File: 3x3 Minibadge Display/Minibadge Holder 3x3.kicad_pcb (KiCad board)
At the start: 2 copper layers, 82.5 x 82.6 mm, 32 parts, among them J1 TYPE-C-31-M-17, SW1 SW_SPDT, U1 AP2112K-3.3, U2 74HC4060, U3 TPM8837C

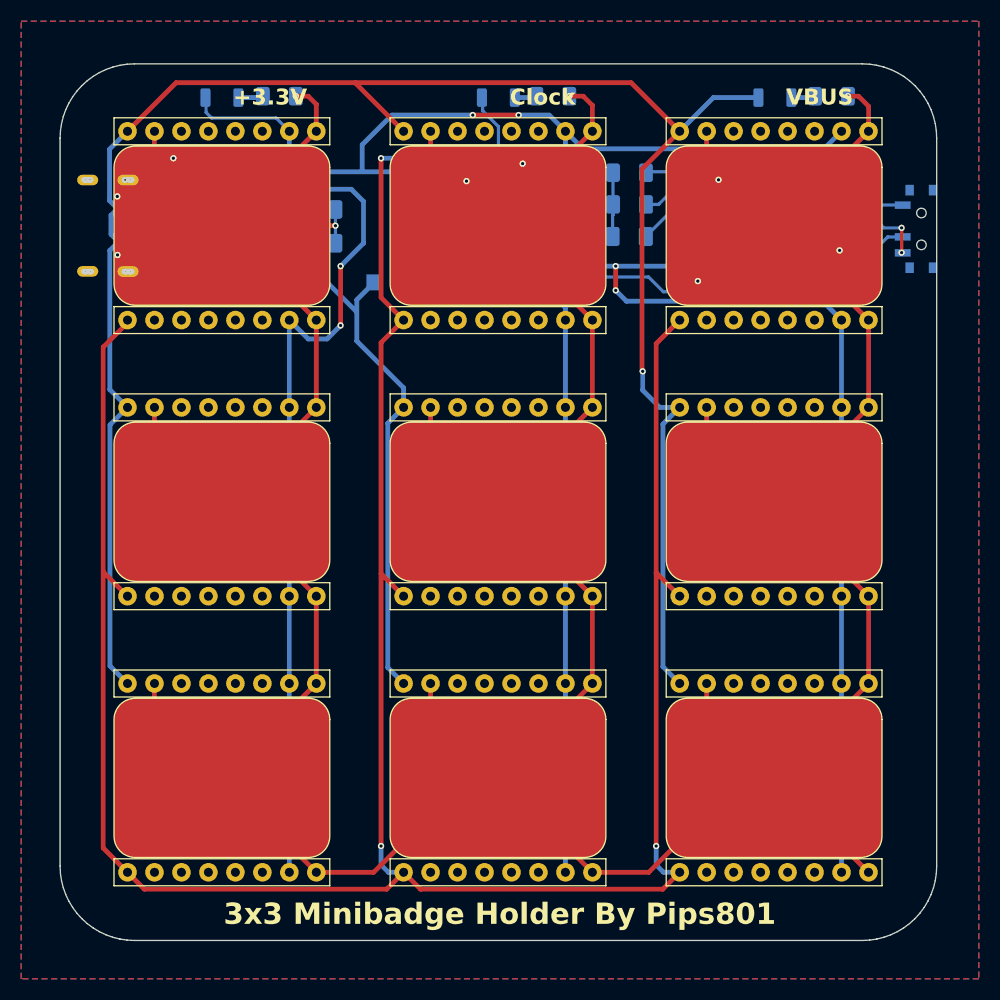
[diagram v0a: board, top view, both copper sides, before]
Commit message: r3 (on/off, graphics, laser cut files)
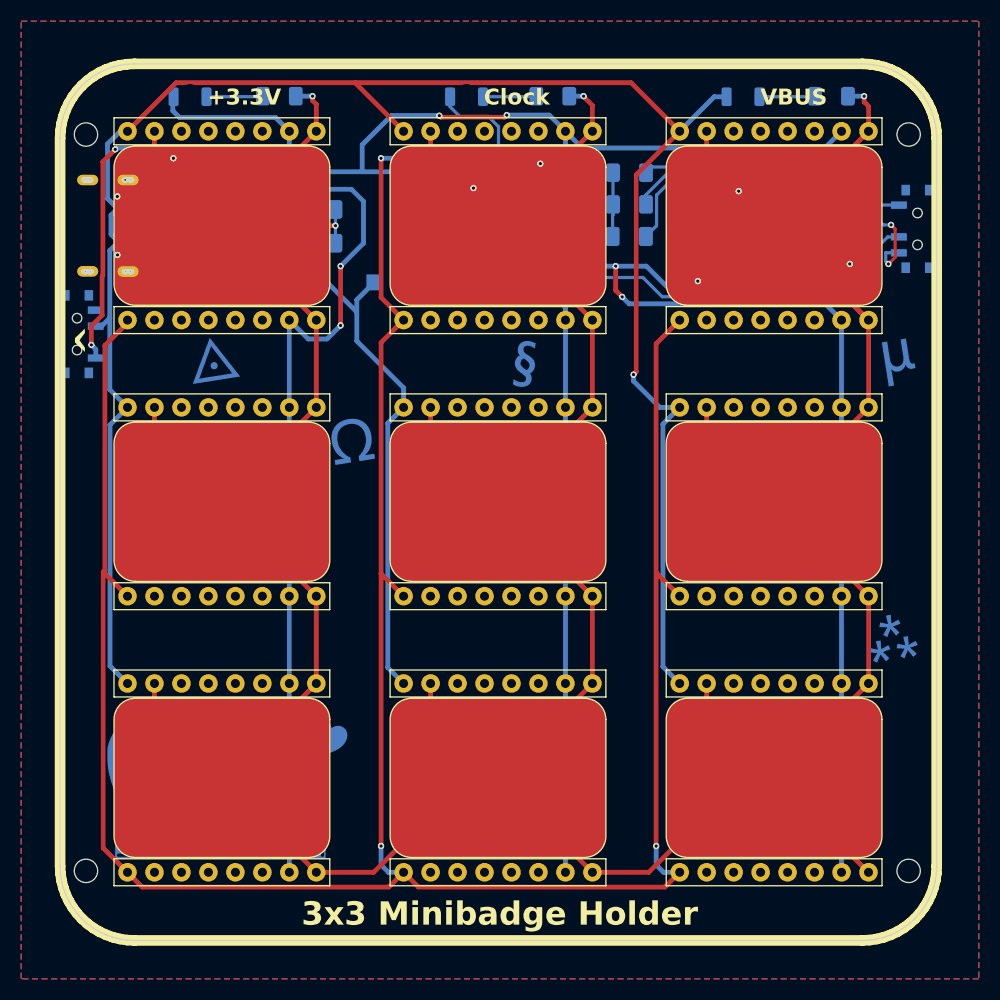
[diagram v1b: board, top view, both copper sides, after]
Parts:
- added G***: LOGO, LOGO, B.Cu at (179.4, 103.0)
- added G***: LOGO, LOGO, B.Cu at (123.5, 118.2)
- added REF**: MountingHole_2.2mm_M2, MountingHole:MountingHole_2.2mm_M2, F.Cu at (191.5, 65.3)
- added REF**: MountingHole_2.2mm_M2, MountingHole:MountingHole_2.2mm_M2, F.Cu at (114.0, 134.6)
- added REF**: MountingHole_2.2mm_M2, MountingHole:MountingHole_2.2mm_M2, F.Cu at (191.5, 134.6)
- added REF**: MountingHole_2.2mm_M2, MountingHole:MountingHole_2.2mm_M2, F.Cu at (114.0, 65.3)
- added SW1: ON/OFF, Button_Switch_SMD:SW_SPDT_PCM12, B.Cu at (113.5, 84.1)
- D1, D2, D3: footprint LED_SMD:LED_1206_3216Metric_ReverseMount_Hole1.8x2.4mm -> Pips Lib:LED_1206_3216Metric_ReverseMount_Hole1.8x2.4mm
- R3, R7: value 5.1k -> 5.1kΩ
- R5: value 20k -> 20kΩ
- SW2: renamed from SW1; value SW_SPDT -> CLOCK SPEED
- U2: value 74HC4060 -> 74HC4060D; footprint Package_SO:SSOP-16_5.3x6.2mm_P0.65mm -> 74LV4060D,118:74LV4060D118
- moved D1 3.00 mm to (123.9, 61.7)
- moved D2 3.00 mm to (175.9, 61.7)
- moved D3 3.00 mm to (149.9, 61.7)
- moved U2 2.28 mm to (176.1, 74.9), turned to 180 degrees
- moved C4 0.95 mm to (186.0, 74.5)
- moved U3 0.91 mm to (152.0, 74.4)
- moved TP4 0.86 mm to (148.2, 68.0)
- moved SW2 0.37 mm to (192.0, 74.2)
- renumbered J1 to USB1
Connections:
- U1 pad 3: VBUS -> Net-(SW1-A)
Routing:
- net Net-(SW1-A): track 0.00 -> 33.3 mm, vias 0 -> 2
- net GND: track 537.4 -> 551.5 mm
- net +3.3V: track 371.1 -> 382.0 mm
- net VBUS: track 266.3 -> 262.5 mm
- net /FAST: track 20.8 -> 17.2 mm
- net Net-(D2-K): track 2.21 -> 5.25 mm
- net CLK_LOW: track 54.8 -> 57.7 mm
- net Net-(D1-K): track 2.42 -> 5.33 mm
- net Net-(D3-K): track 2.14 -> 5.05 mm
- net /SLOW: track 24.4 -> 21.9 mm
- net Net-(U2-~{Φ1}): track 8.78 -> 10.1 mm
- net Net-(U2-~{Φ0}): track 9.70 -> 10.6 mm
- net Net-(U2-Φ0): track 9.30 -> 10.0 mm
- added copper zone on B.Cu, net (none)
- removed copper zone on B.Cu, net GND
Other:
- board text added: "! Reflective pads on the front are GROUND ! Make sure that no minibadge components are shorting against it."
- board text added: "${TITLE}"
- board text added: "74LV4060D"
- board text added: "AP2112K"
- board text added: "^"
